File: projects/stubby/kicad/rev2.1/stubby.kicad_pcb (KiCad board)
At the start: 2 copper layers, 49.5 x 49.5 mm, 72 parts, among them IC1 ATMEGA1284-A, P1 CONN_6, P10 CONN_4, P11 CONN_6, P2 CONN_6, P3 CONN_10, P4 CONN_13, P5 CONN_4, P6 CONN_2, P7 CONN_1, P8 BATT (4.8V-6V), P9 PROG, SW1 SW_PUSH, SW2 DPDT, U1 HMC5883L, X1 CRYSTAL

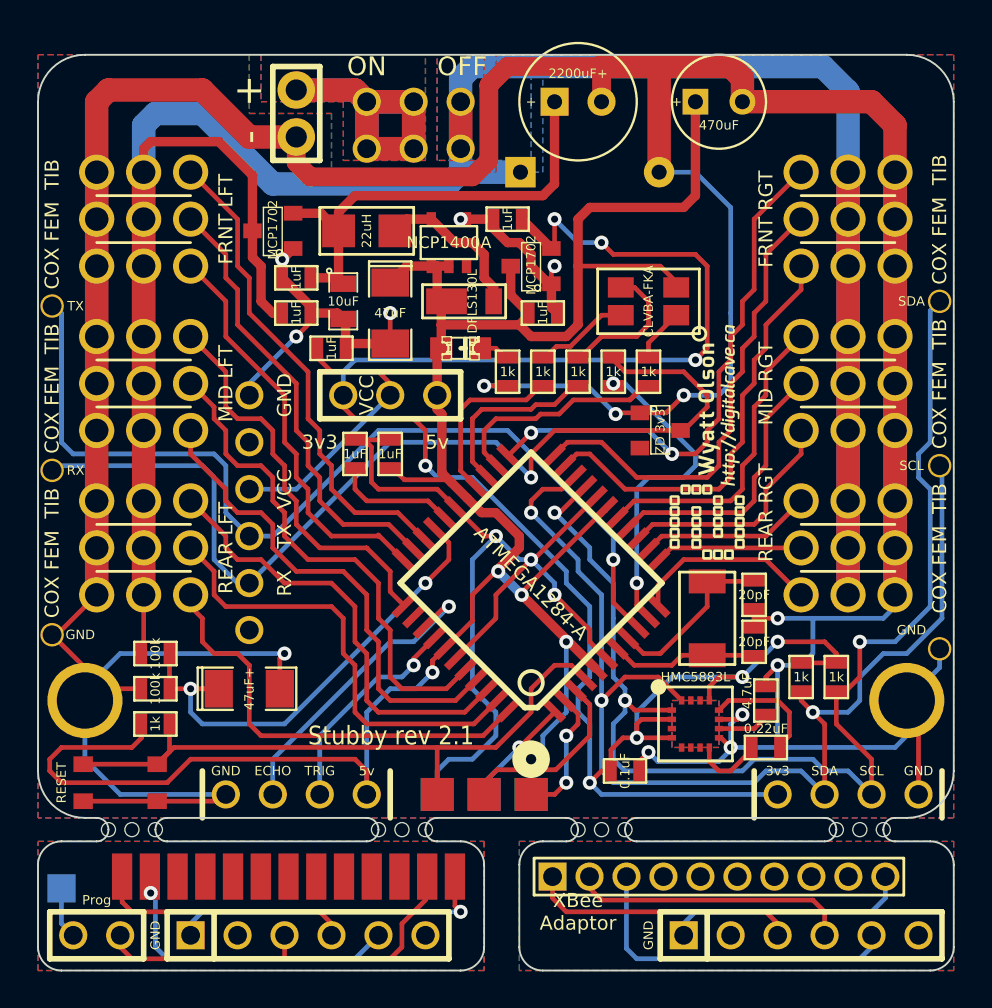
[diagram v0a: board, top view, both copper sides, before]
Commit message: -Renamed hex.* to stubby.* (why I didn't do this sooner, who knows...) -Work on improving the continuity of the ground plane (back layer) -Moving all through hole capacitors to the back of the board, laying flat
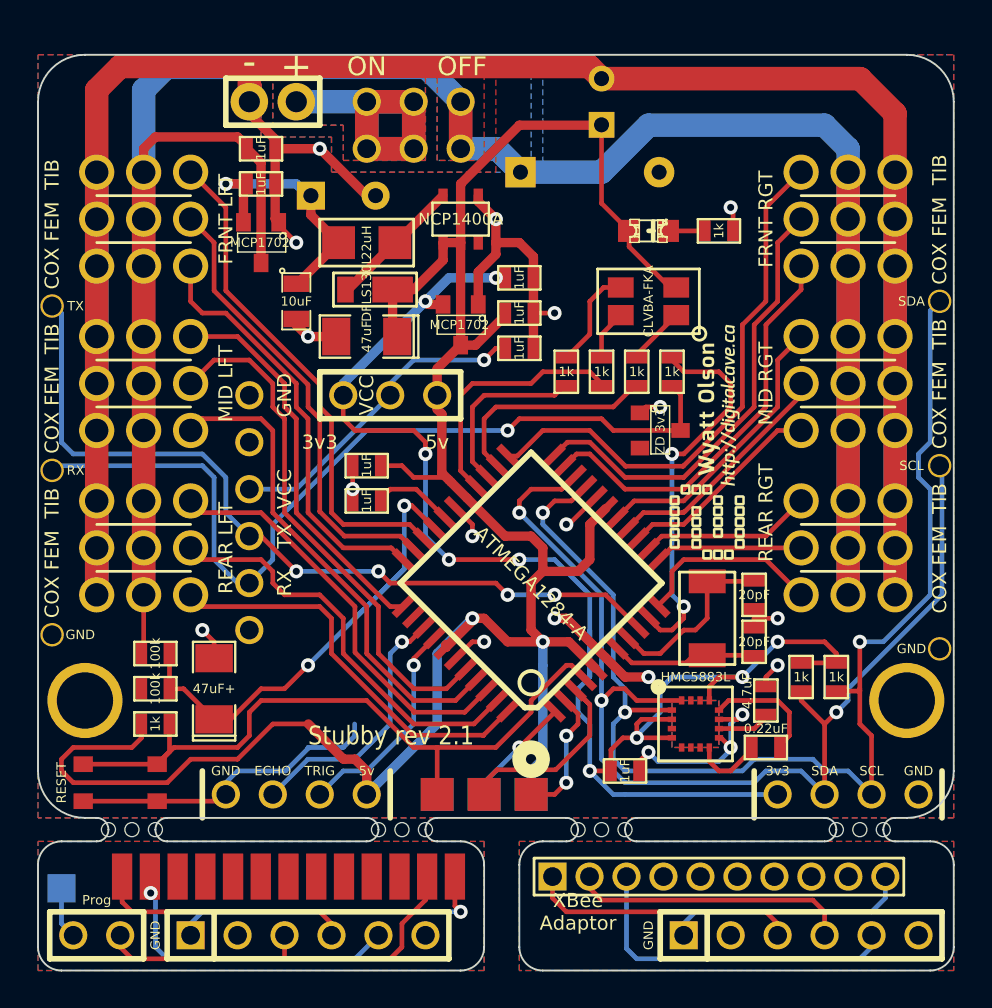
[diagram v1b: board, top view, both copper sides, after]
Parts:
- C11, C2: moved to B.Cu
- C19: value 0.1uF -> 1uF
- moved R4 13.7 mm to (72.4, 24.1), turned to 180 degrees
- moved C2 13.7 mm to (52.1, 22.2)
- moved D2 12.0 mm to (68.6, 24.1)
- moved C16 10.2 mm to (61.6, 30.5)
- moved C4 9.09 mm to (47.6, 19.7)
- moved C11 6.35 mm to (66.0, 17.1), turned to 90 degrees
- moved D1 5.75 mm to (53.3, 27.3), turned to 0 degrees
- moved C3 5.43 mm to (47.6, 21.6), turned to 0 degrees
- moved VR3 4.96 mm to (58.4, 29.2), turned to 180 degrees
- moved C13 3.24 mm to (61.6, 26.7), turned to 0 degrees
- moved R8 3.18 mm to (66.0, 31.8)
- moved R7 3.17 mm to (69.8, 31.8), turned to 270 degrees
- moved C5 2.62 mm to (53.3, 38.7), turned to 0 degrees
- moved C1 2.54 mm to (49.5, 27.9)
- moved C15 1.91 mm to (45.1, 48.9), turned to 90 degrees
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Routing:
- net GND: track 359.4 -> 225.3 mm, vias 17 -> 19
- net +3.3V: track 107.6 -> 85.4 mm, vias 8 -> 9
- net N-0000085: track 25.5 -> 14.5 mm, vias 0 -> 1
- net +BATT: track 166.1 -> 157.2 mm
- net /MODULE_RX: track 53.7 -> 47.0 mm
- net /AVR_RX: track 58.8 -> 52.8 mm, vias 1 -> 4
- net /BATTERY: track 28.5 -> 24.1 mm
- net /LED_GR: track 9.57 -> 13.9 mm
- net /RESET: track 35.4 -> 38.9 mm
- net /AVR_TX: track 17.6 -> 21.1 mm
- net /LED_GR_R: track 5.17 -> 2.73 mm
- net /ADC_BATTERY_METER: track 25.7 -> 28.1 mm
- net /DIST_ECHO: track 16.6 -> 14.2 mm
- net /AREF: track 6.73 -> 4.52 mm
- net /LED_BL_R: track 7.63 -> 5.56 mm
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
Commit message: Simplified a few traces in the power supply; moved battery indicator capacitor to be further from the rails
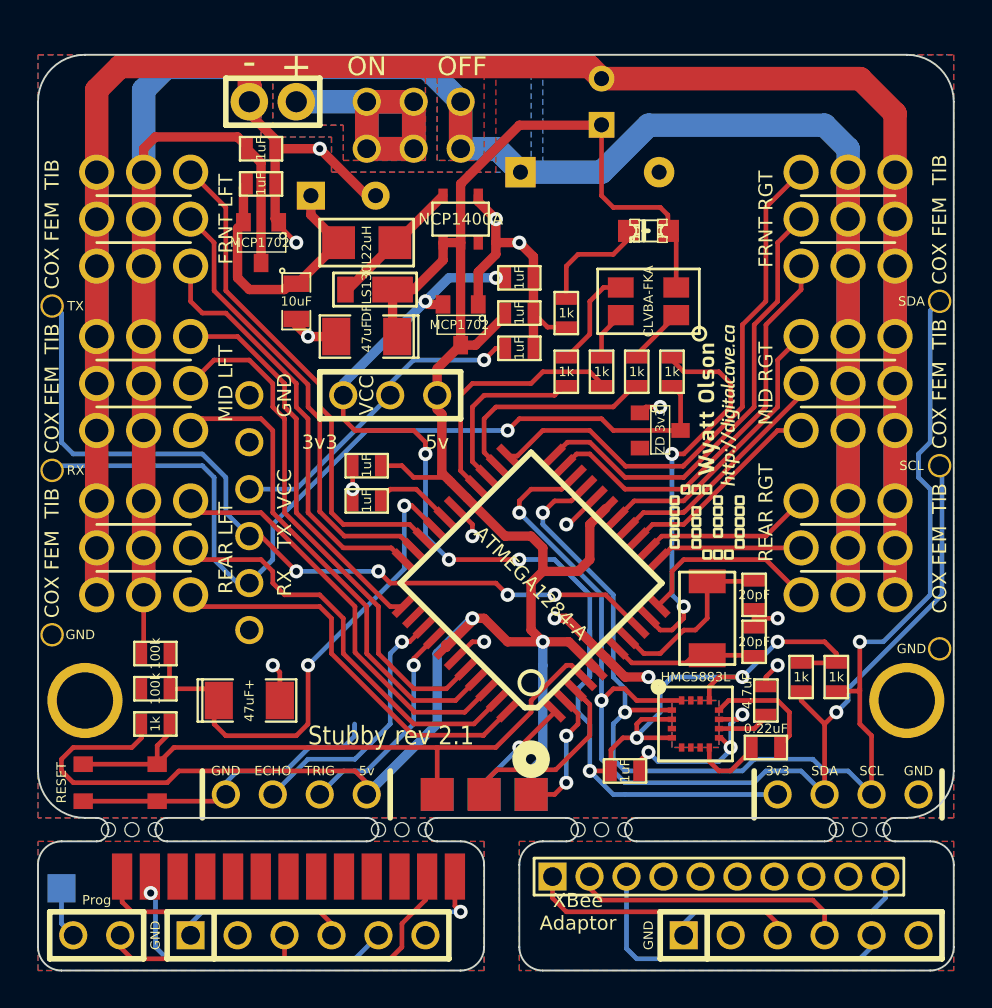
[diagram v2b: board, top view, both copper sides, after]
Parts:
- moved R4 9.38 mm to (64.1, 28.6), turned to 90 degrees
- moved C15 2.01 mm to (47.0, 49.5), turned to 0 degrees
- turned D2 to 180 degrees
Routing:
- net N-0000015: track 2.00 -> 6.21 mm
- net /RESET: track 38.9 -> 36.1 mm
- net +5V: track 128.0 -> 126.8 mm
- net N-0000085: track 14.5 -> 15.2 mm, vias 1 -> 0
- net GND: track 225.3 -> 225.2 mm, vias 19 -> 18

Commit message: Updated Stubby 2.1 to use (almsot) all SMD components
Only through hole components remaining are headers and the power switch.
The big servo capacitor is on the bottom, though.
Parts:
- removed C2: 2200uF+, C1V7
- removed ZD1: ZD 3v3, SOT23
- added R11: 2k, SM0603_VALUE, F.Cu at (67.9, 34.9)
- C11: footprint C1V5 -> c_elec_5x5.3; moved to F.Cu
- C17: value 15000µF -> 6800µF; footprint C1V8 -> c_elec_18x18
- SW1: footprint sw_42_32 -> SW_6x3
- moved C17 19.1 mm to (60.3, 39.4), turned to 90 degrees
- moved C11 1.42 mm to (65.4, 18.4), turned to 270 degrees
- moved P9 1.27 mm to (58.4, 57.1)
- moved P3 0.63 mm to (72.4, 58.4)
- moved SW1 0.63 mm to (40.0, 53.3), turned to 0 degrees
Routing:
- net GND: track 225.2 -> 210.9 mm, vias 18 -> 17
- net +BATT: track 157.2 -> 168.7 mm
- net +5V: track 126.8 -> 119.2 mm, vias 2 -> 4
- net N-0000080: track 15.2 -> 12.1 mm
- net /RESET: track 36.1 -> 38.3 mm, vias 0 -> 2
- net /MOSI: track 6.29 -> 8.30 mm
- net N-0000027: track 18.3 -> 16.4 mm
- net /MODULE_RX: track 47.0 -> 45.2 mm
- net /SCK: track 11.4 -> 12.7 mm
- net /MISO: track 7.24 -> 8.51 mm
- net N-0000026: track 15.1 -> 15.8 mm
- net N-0000025: track 14.5 -> 15.2 mm
- net /XBEE_GND: track 13.3 -> 13.9 mm
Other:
- board text removed: "XBee Adaptor"

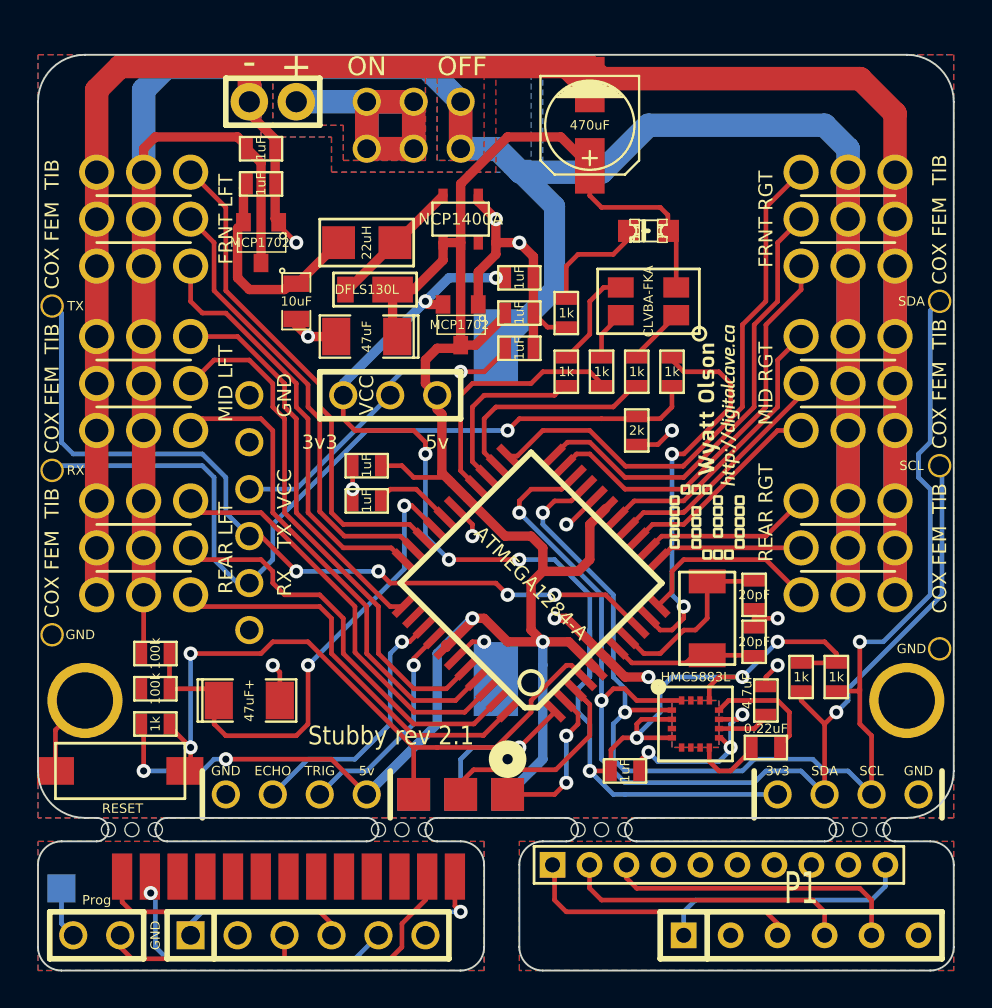
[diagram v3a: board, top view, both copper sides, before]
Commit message: Re-added a smaller capacitor to +BATT
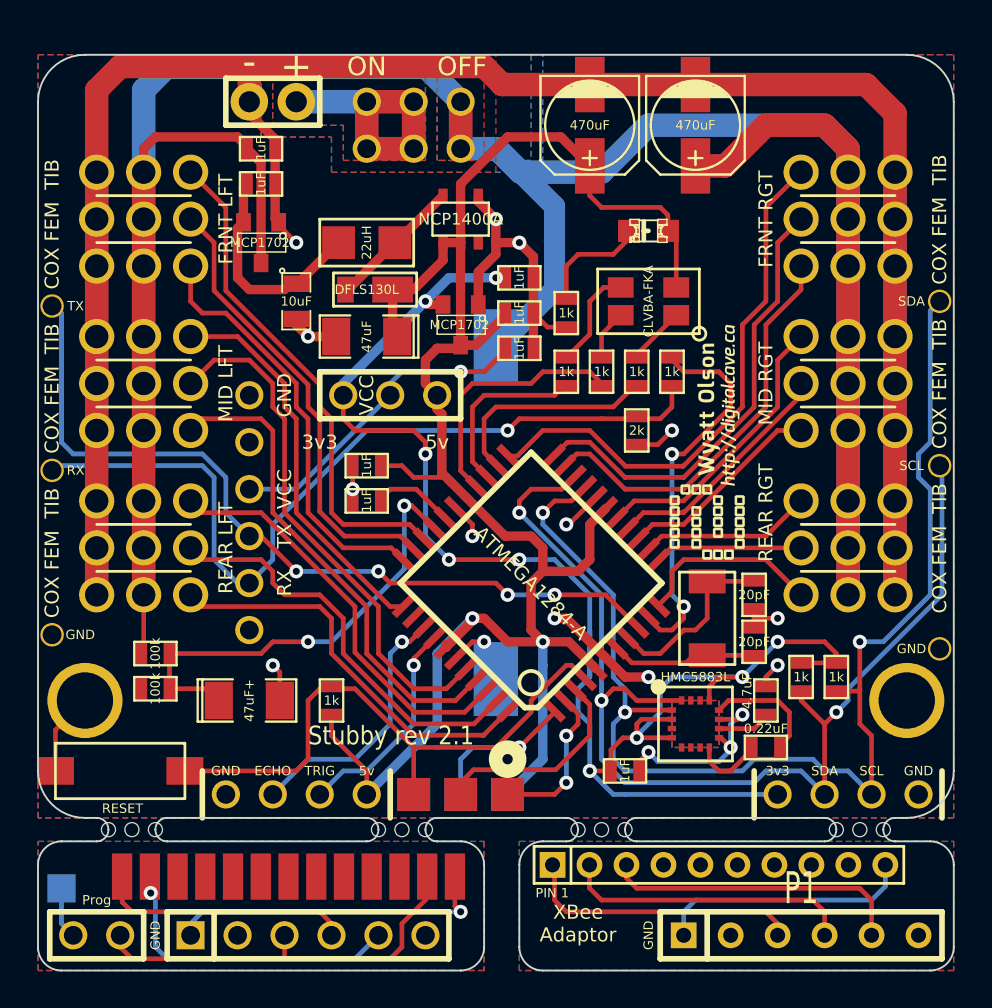
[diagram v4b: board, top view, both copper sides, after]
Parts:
- added C2: 470uF, c_elec_5x5.3, F.Cu at (71.1, 18.4)
- moved R3 9.61 mm to (51.4, 49.5), turned to 90 degrees
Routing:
- net +BATT: track 168.7 -> 179.7 mm
- net +5V: track 119.2 -> 108.6 mm, vias 4 -> 2
- net /RESET: track 38.3 -> 32.9 mm, vias 2 -> 0
- net /ADC_BATTERY_METER: track 28.0 -> 25.1 mm
- net GND: track 210.9 -> 209.2 mm
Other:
- board text added: "PIN 1"
- board text added: "XBee Adaptor"

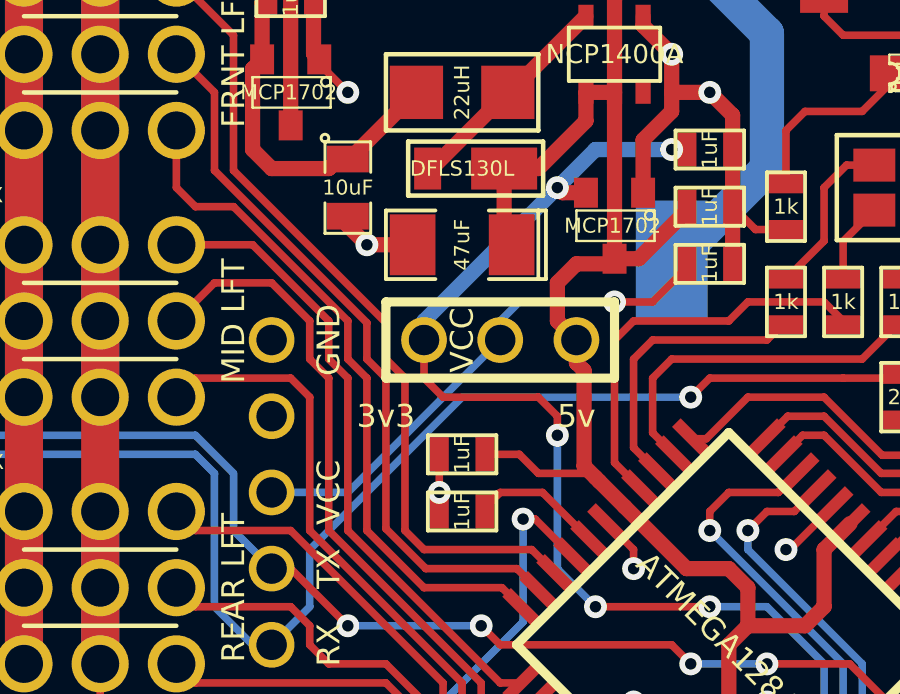
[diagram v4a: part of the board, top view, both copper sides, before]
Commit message: Removed the 5v / 3.3v selector jumper from the rev 2.1 board.  It just complicates things.  Use a 3.3v FTDI cable if you want a hard-wired connection.
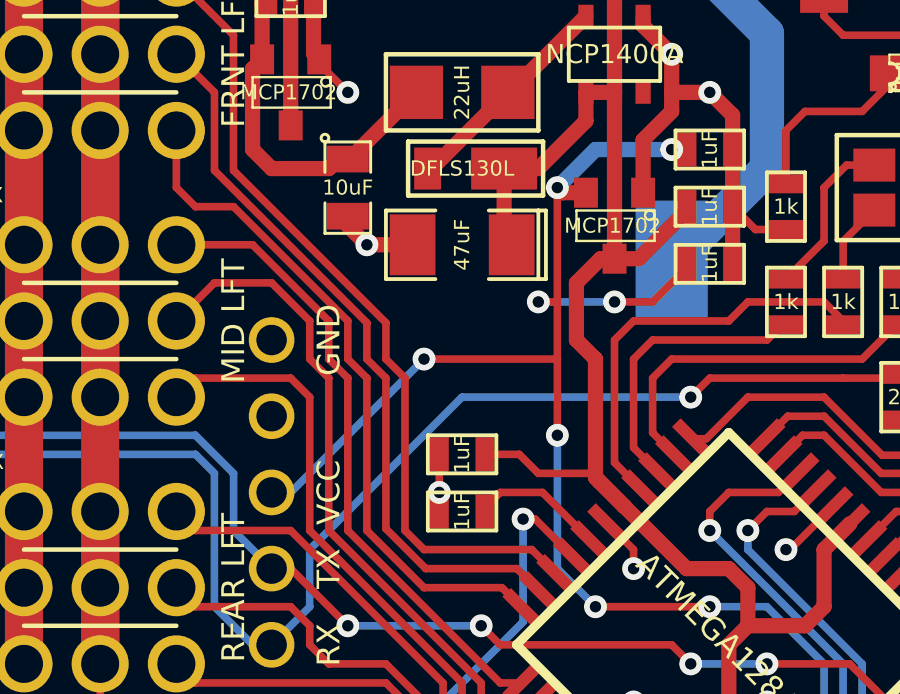
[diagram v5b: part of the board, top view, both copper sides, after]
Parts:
- removed JP1: CONN_3, SIL-3
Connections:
- C16 pad 2: N-0000077 (its old number) -> +3.3V
- P11 pad 3: N-0000077 (its old number) -> +3.3V
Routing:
- net N-0000077 (its old number): track 17.4 -> 0.00 mm, vias 1 -> 0
- net +3.3V: track 85.4 -> 97.4 mm, vias 9 -> 12
